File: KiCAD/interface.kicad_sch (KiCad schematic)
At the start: 3 parts, among them J4 8P8C_Shielded

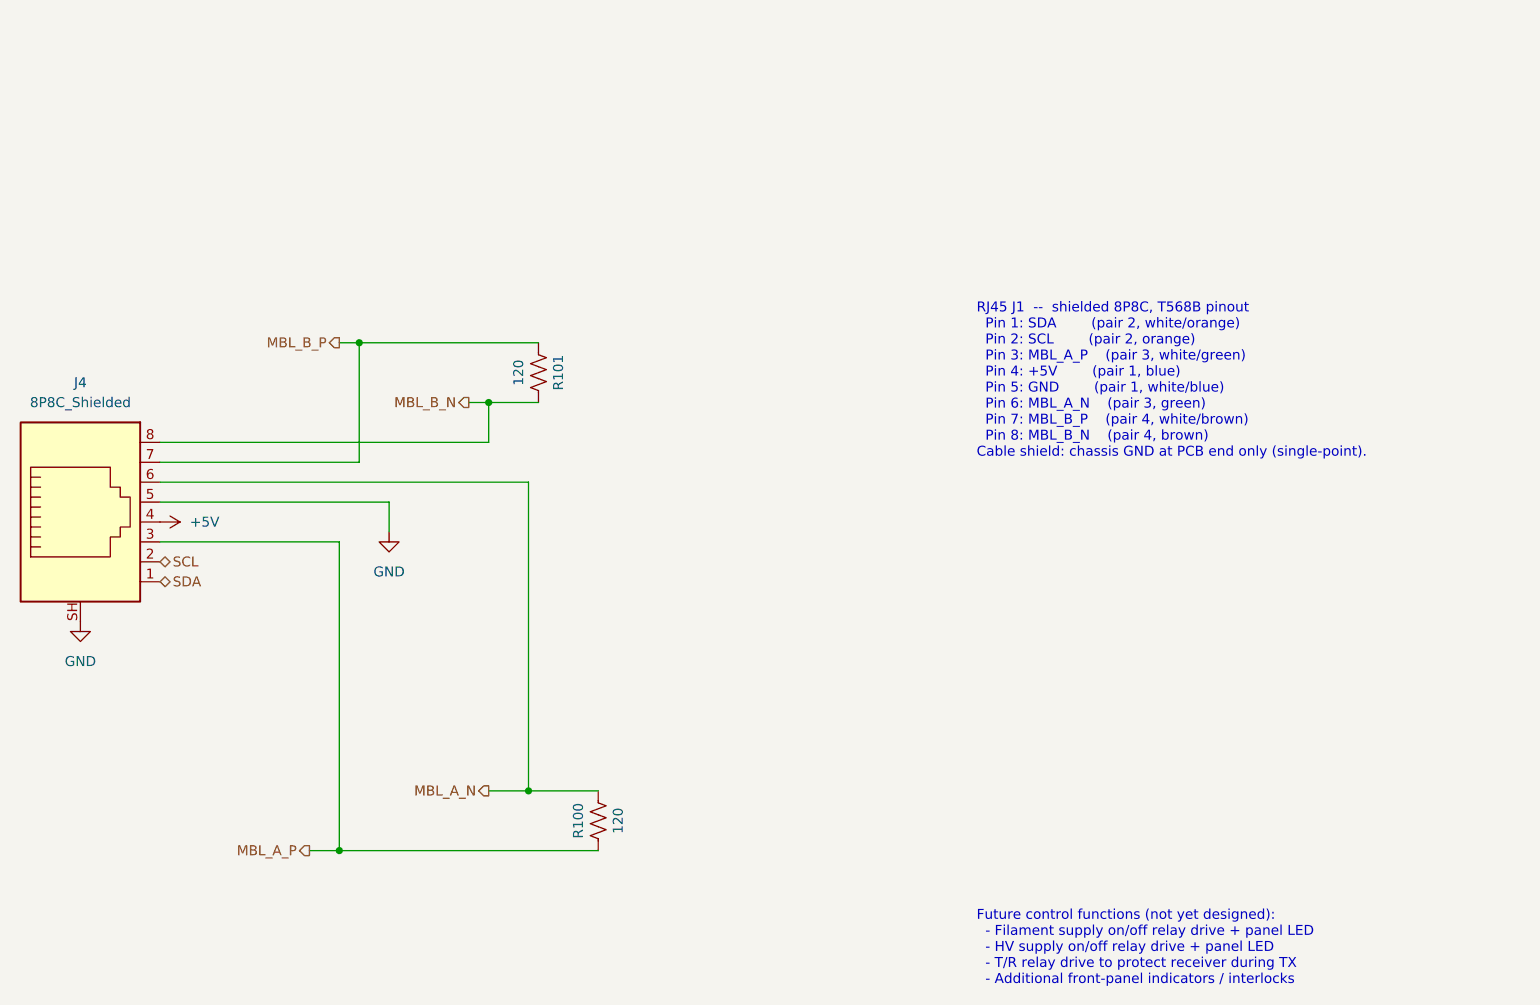
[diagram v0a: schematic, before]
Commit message: interface+arduino: wire the MBL-600 signal chain end-to-end
Interface sheet — receiver + termination + level-shift, all live:
  - RJ45 J1 (shielded 8P8C, Connector library symbol) instantiated with
    hierarchical labels on all eight positions per T568B; RJ45 pins
    3/6/7/8 land on MBL_A_P/N and MBL_B_P/N at the receiver-input side
  - R100 = R101 = 120 Ohm across the differential pairs (RS-422
    termination at the receiver end)
  - AM26LS32ACN (U15) at (119.38, 104.14); ch 1 handles MBL_A±, ch 2
    handles MBL_B±
  - Both enable pins tied to GND. ~G at pin 4 is the active-LOW
    enable, so GND puts it in its active state and turns on all four
    receivers per the datasheet's OR-logic gate (the other enable at
    pin 12 stays inactive at GND, but that is fine -- either one active
    is enough). GND was chosen over VCC purely for routing ease --
    GND fill will be closer than +5V traces at layout time
  - 2.2K + 10K voltage divider on each channel output (R26+R28 for A,
    R27+R29 for B). Ratio 10/12.2 = 0.82 drops the ~3.4 V TTL to
    ~2.79 V at the divider midpoint, comfortably below the ESP32
    absolute-max of 3.6 V and comfortably above V_IH_min (~2.475 V)
  - MBL600_A and MBL600_B hierarchical labels attached at the divider
    midpoints (not at the receiver 1Y/2Y pins) so the divided signal is
    what leaves the sheet
  - VCC (pin 16) wired to +5V, bypassed by 10 uF electrolytic + 100 nF
    ceramic (datasheet requires only 0.1 uF minimum; the 10 uF is
    just bonus bulk)
  - Unused channels 3&4 A/B inputs and 3Y/4Y outputs left unconnected
    per datasheet allowance

Arduino sheet:
  - MBL600_A hierarchical label at Metro D2, MBL600_B at Metro D3 --
    matches the FREQ_A / FREQ_B slots that the Metro symbol reserved
  - I_CATHODE_A moved from A0 (ADC2) to D8 (ADC1)
  - I_CATHODE_B moved from A1 (ADC2) to D9 (ADC1) -- both now on ADC1
    per the cathode-monitor design decision; the old A0/A1 assignment
    would have conflicted with WiFi/BL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
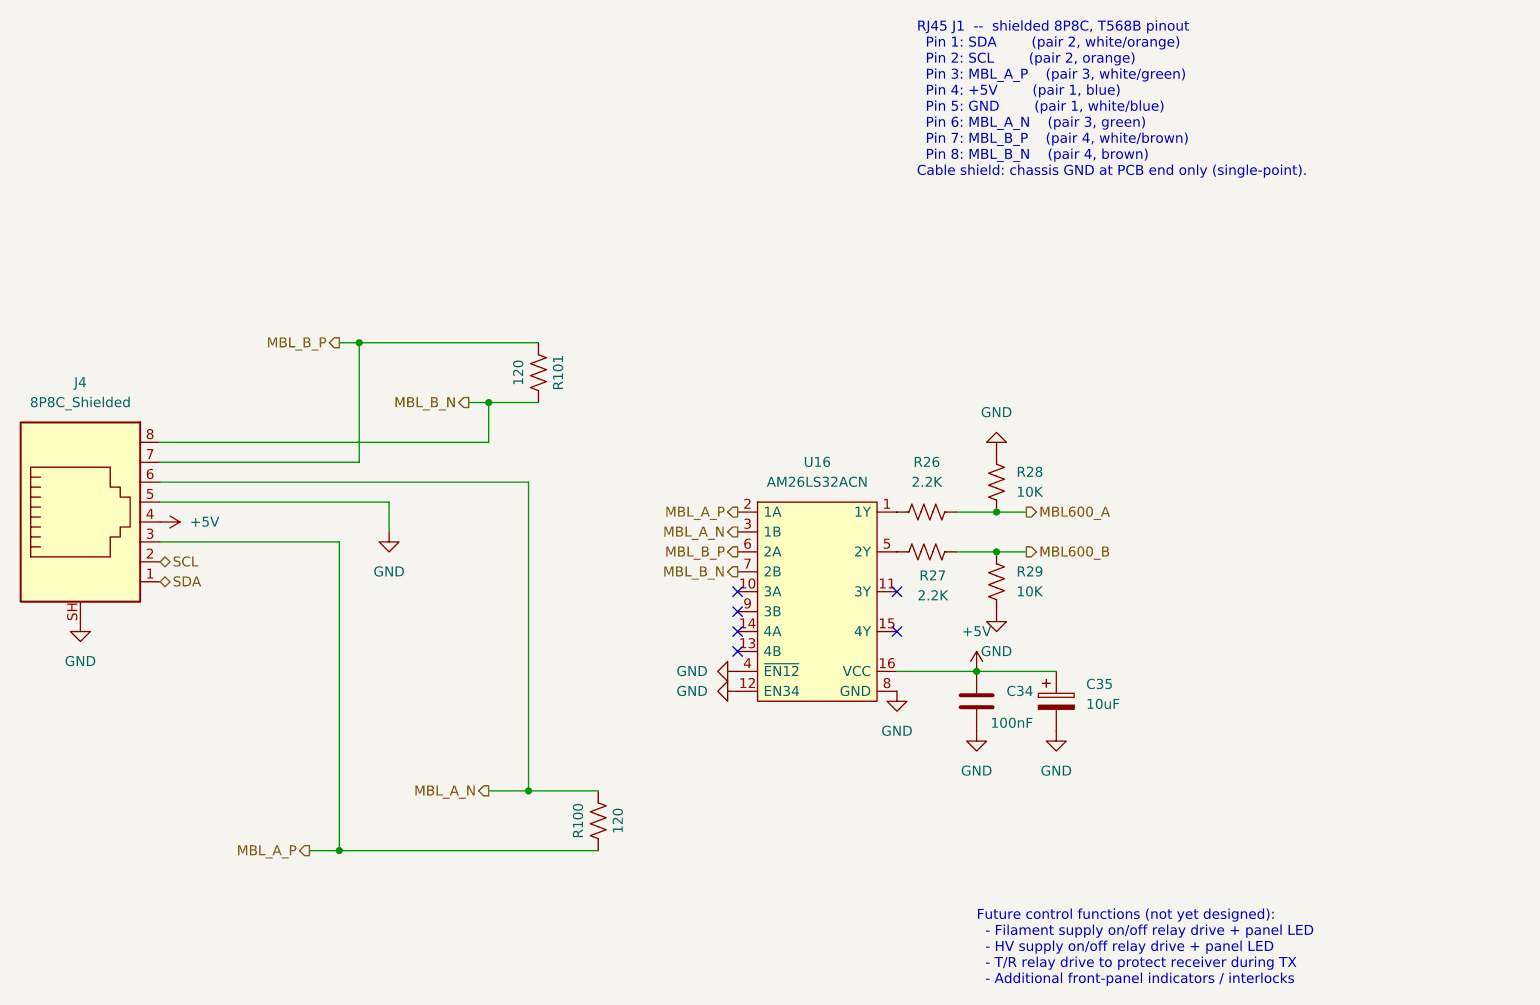
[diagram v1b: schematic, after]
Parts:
- added C34: 100nF, symbol Device:C
- added C35: 10uF, symbol Device:C_Polarized
- added R26, R27: 2.2K, symbol Device:R_US
- added R28, R29: 10K, symbol Device:R_US
- added U16: AM26LS32ACN, Package_DIP:DIP-16_W7.62mm, symbol xmitter:AM26LS32ACN
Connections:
- net +5V: now also C34.1, C35.1, U16.16 (VCC)
- net GND: now also C34.2, C35.2, R28.1, R29.2, U16.12 (EN34), U16.4 (~{EN12}), U16.8 (GND)
- net MBL_A_N: now also U16.3 (1B)
- net MBL_A_P: now also U16.2 (1A)
- net MBL_B_N: now also U16.7 (2B)
- net MBL_B_P: now also U16.6 (2A)
- new net: R26.1, U16.1 (1Y)
- new net: R27.1, U16.5 (2Y)
- new net MBL600_A: R26.2, R28.2
- new net MBL600_B: R27.2, R29.1
- no-connect marks 0 -> 6

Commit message: kicad: fill missing footprints across active sheets + MCP4728 breakout footprint
Footprint sweep across the analog control board sheets. All active sheets
now clean except U2 (Metro), which is intentionally off-PCB per the
Wingshield-plus-jumpers connection strategy.

Auto-assigned via tools/assign_cap_footprints.py:
  - buffer_keyer: C39, C40 (100 nF, THT disc D5.0mm P5.00mm) -- the null-
    trim bypass caps at R_INJ1 / R_INJ2 that ground the DAC output side
    of the 330K injection resistors going into T1 and T2
  - arduino: C36, C38 (100 nF THT disc), C37 (10 uF radial electrolytic)
  - interface: C34 (100 nF), C35 (10 uF)

Manual assignments:
  - interface: R26, R27, R28, R29 -> R_Axial_DIN0207_L6.3mm axial THT
    (matching the other 1/4W metal-film resistors used throughout)
  - interface: J4 (RJ45 socket) -> xmitter:Amphenol_RJE1D-188_Horizontal_Shielded
  - arduino: J6, J7, J8, J9, J10 -> PinHeader_1x02_P2.54mm_Vertical
  - buffer_keyer: U8 (MCP4728 breakout) -> new custom footprint

New custom footprint xmitter:Adafruit_MCP4728_Breakout:
  - Board 1.00 x 0.70 in (25.4 x 17.78 mm)
  - Four NPTH 2.5 mm mounting holes on 0.80 x 0.50 in spacing
  - 10 THT pads in two rows of 5, pad numbers match the xmitter:MCP4728
    symbol (1=VIN, 2=GND, 3=SCL, 4=SDA, 5=LDAC, 6=RDY, 7=VA, 8=VB, 9=VC,
    10=VD)
  - Pins 3 (SCL) and 4 (SDA) will be left unrouted on the parent PCB
    per the STEMMA QT daisy-chain topology decision -- I2C reaches the
    MCP4728 via a STEMMA cable from the Si5351 breakout, not via PCB
    traces
  - descr field flags "VERIFY silk-label to pad-number correspondence
    against the physical breakout before routing" -- Adafruit revisions
    vary and the specific row assignment was inferred from the
    datasheet fab print on page 20 plus the symbol pin numbering

Also committing Documentation/Components/MCP4728_datasheet.pdf and
Documentation/Components/cd4050b.pdf datasheets that were sitting
uncommitted.

Co-Authored-By: Claude Opus 4.7 <nor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
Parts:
- C34: footprint (none) -> Capacitor_THT:C_Disc_D5.0mm_W2.5mm_P5.00mm
- C35: footprint (none) -> Capacitor_THT:CP_Radial_D5.0mm_P2.00mm
- J4: footprint (none) -> xmitter:Amphenol_RJE1D-188_Horizontal_Shielded
- R26, R27, R28, R29: footprint (none) -> Resistor_THT:R_Axial_DIN0207_L6.3mm_D2.5mm_P10.16mm_Horizontal
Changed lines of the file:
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@@
 			)
 		)
-		(property "Footprint" ""
+		(property "Footprint" "Resistor_THT:R_Axial_DIN0207_L6.3mm_D2.5mm_P10.16mm_Horizontal"
 			(at 133.604 91.694 90)
 			(hide yes)
@@
 			)
 		)
-		(property "Footprint" ""
+		(property "Footprint" "Resistor_THT:R_Axial_DIN0207_L6.3mm_D2.5mm_P10.16mm_Horizontal"
 			(at 133.604 96.774 90)
 			(hide yes)
@@
 			)
 		)
-		(property "Footprint" ""
+		(property "Footprint" "Resistor_THT:R_Axial_DIN0207_L6.3mm_D2.5mm_P10.16mm_Horizontal"
 			(at 143.256 101.854 90)
 			(hide yes)
@@
 			)
 		)
-		(property "Footprint" ""
+		(property "Footprint" "Capacitor_THT:CP_Radial_D5.0mm_P2.00mm"
 			(at 150.8252 120.65 0)
 			(hide yes)
@@
 			)
 		)
-		(property "Footprint" ""
+		(property "Footprint" "Capacitor_THT:C_Disc_D5.0mm_W2.5mm_P5.00mm"
 			(at 140.6652 120.65 0)
 			(hide yes)
@@
 			)
 		)
-		(property "Footprint" ""
+		(property "Footprint" "Resistor_THT:R_Axial_DIN0207_L6.3mm_D2.5mm_P10.16mm_Horizontal"
 			(at 143.256 89.154 90)
 			(hide yes)
@@
 			)
 		)
-		(property "Footprint" ""
+		(property "Footprint" "xmitter:Amphenol_RJE1D-188_Horizontal_Shielded"
 			(at 25.4 93.345 90)
 			(hide yes)

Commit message: schematic: I2C topology flip + CD14538B heartbeat + pre-layout audit
- Documentation updates for the STEMMA-QT topology flip (MCP4728 upstream
  of Si5351): design_review_7-5-26 C1 marked resolved, build_checklist
  Phase 1 gets the 6-step first-boot procedure, cw_envelope_keyer I2C
  address section rewritten, front_panel_interface signal-chain diagram
  refreshed.
- CD14538B dual retriggerable monostable added to xmitter.kicad_sym
  (PDIP-16, pinout verified against datasheet fig. 1), plus datasheet
  file.
- Arduino sheet: CD14538B heartbeat topology on Q5 HV contactor -- U18
  + R30 470K + C41 1uF timing (t_w ~470 ms), Q7 series FET stack,
  C42/C43 VDD bypass and bulk.
- Pre-layout audit output as Documentation/punch_list_7-6-26.txt (list
  of blockers before PCB layout, ordered by severity).

Co-Authored-By: Claude Opus 4.7 (1M context) <noreply@anthropic.com>
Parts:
- added J15: Conn_01x03_Pin, symbol Connector:Conn_01x03_Pin
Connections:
- net GND: now also J15.1 (Pin_1)
- net MBL600_A: now also J15.3 (Pin_3)
- net MBL600_B: now also J15.2 (Pin_2)
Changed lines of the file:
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@@
+	)
+	(junction
+		(at 151.13 97.79)
+		(diameter 0)
+		(color 0 0 0 0)
+	)
+	(junction
+		(at 170.18 92.71)
+		(diameter 0)
+		(color 0 0 0 0)
 	)
 	(junction
@@
 	)
 	(junction
-		(at 142.24 97.79)
+		(at 142.24 92.71)
 		(diameter 0)
 		(color 0 0 0 0)
@@
 	)
 	(junction
-		(at 142.24 92.71)
+		(at 142.24 97.79)
 		(diameter 0)
 		(color 0 0 0 0)
@@
 	(wire
 		(pts
-			(xy 146.05 92.71) (xy 142.24 92.71)
+			(xy 173.99 92.71) (xy 170.18 92.71)
+		)
+		(stroke
+			(width 0)
+			(type default)
+		)
+	)
+	(wire
+		(pts
+			(xy 170.18 92.71) (xy 170.18 102.87)
 		)
 		(stroke
@@
 	(wire
 		(pts
+			(xy 151.13 97.79) (xy 142.24 97.79)
+		)
+		(stroke
+			(width 0)
+			(type default)
+		)
+	)
+	(wire
+		(pts
 			(xy 64.77 91.44) (xy 64.77 95.25)
 		)
@@
 	(wire
 		(pts
+			(xy 170.18 92.71) (xy 142.24 92.71)
+		)
+		(stroke
+			(width 0)
+			(type default)
+		)
+	)
+	(wire
+		(pts
 			(xy 35.56 96.52) (xy 58.42 96.52)
 		)
@@
 	(wire
 		(pts
-			(xy 146.05 97.79) (xy 142.24 97.79)
+			(xy 153.67 97.79) (xy 151.13 97.79)
+		)
+		(stroke
+			(width 0)
+			(type default)
+		)
+	)
+	(wire
+		(pts
+			(xy 151.13 105.41) (xy 151.13 97.79)
 		)
 		(stroke
@@
 		(pts
 			(xy 58.42 96.52) (xy 58.42 135.89)
+		)
+		(stroke
+			(width 0)
+			(type default)
+		)
+	)
+	(wire
+		(pts
+			(xy 170.18 105.41) (xy 151.13 105.41)
 		)
 		(stroke
@@
 	(hierarchical_label "MBL600_B"
 		(shape output)
-		(at 146.05 97.79 0)
+		(at 153.67 97.79 0)
 		(effects
 			(font
@@
 	(hierarchical_label "MBL600_A"
 		(shape output)
-		(at 146.05 92.71 0)
+		(at 173.99 92.71 0)
 		(effects
 			(font
@@
 					(unit 1)
 				)
+			)
+		)
+	)
+	(symbol
+		(lib_id "Connector:Conn_01x03_Pin")
+		(at 175.26 105.41 180)
+		(unit 1)
+		(body_style 1)
+		(exclude_from_sim no)
+		(in_bom yes)
+		(on_board yes)
+		(in_pos_files yes)
+		(dnp no)
+		(fields_autoplaced yes)
+		(property "Reference" "J15"
+			(at 176.53 104.1399 0)
+			(show_name no)
+			(do_not_autoplace no)
+			(effects
+				(font
+					(size 1.27 1.27)
+				)
+				(justify right)
+			)
+		)
+		(property "Value" "Conn_01x03_Pin"
+			(at 176.53 106.6799 0)
+			(show_name no)
+			(do_not_autoplace no)
+			(effects
+				(font
+					(size 1.27 1.27)
+				)
+				(justify right)
+			)
+		)
+		(property "Footprint" ""
+			(at 175.26 105.41 0)
+			(hide yes)
+			(show_name no)
+			(do_not_autoplace no)
+			(effects
+				(font
+					(size 1.27 1.27)
+				)
+			)
+		)
+		(property "Datasheet" ""
+			(at 175.26 105.41 0)
+			(hide yes)
+			(show_name no)
+			(do_not_autoplace no)
+			(effects
+				(font
+					(size 1.27 1.27)
+				)
+			)
+		)
+		(property "Description" "Generic connector, single row, 01x03, script generated"
+			(at 175.26 105.41 0)
+			(hide yes)
+			(show_name no)
+			(do_not_autoplace no)
+			(effects
+				(font
+					(size 1.27 1.27)
+				)
+			)
+		)
+		(pin "2"
+		)
+		(pin "1"
+		)
+		(pin "3"
+		)
+		(instances
+			(project "KiCAD"
+				(path "/d3de40b8-856b-4fbd-829c-f45ffcd55742/5c3f4a2b-7d1e-4f8b-9c6d-0e8a1b2c3d4e"
+					(reference "J15")
+					(unit 1)
+				)
+			)
+		)
+	)
+	(symbol
+		(lib_id "power:GND")
+		(at 170.18 107.95 0)
+		(unit 1)
+		(body_style 1)
+		(exclude_from_sim no)
+		(in_bom yes)
+		(on_board yes)
+		(in_pos_files yes)
+		(dnp no)
+		(fields_autoplaced yes)
+		(property "Reference" "#PWR0119"
+			(at 170.18 114.3 0)
+			(hide yes)
+			(show_name no)
+			(do_not_autoplace no)
+			(effects
+				(font
+					(size 1.27 1.27)
+				)
+			)
+		)
+		(property "Value" "GND"
+			(at 170.18 113.03 0)
+			(show_name no)
+			(do_not_autoplace no)
+			(effects
+				(font
+					(size 1.27 1.27)
+				)
+			)
+		)
+		(property "Footprint" ""
+			(at 170.18 107.95 0)
+			(hide yes)
+			(show_name no)
+			(do_not_autoplace no)
+			(effects
+				(font
+					(size 1.27 1.27)
+				)
+			)
+		)
+		(property "Datasheet" ""
+			(at 170.18 107.95 0)
+			(hide yes)
+			(show_name no)
+			(do_not_autoplace no)
+			(effects
+				(font
+					(size 1.27 1.27)
+				)
+			)
+		)
+		(property "Description" "Power symbol creates a global label with name \"GND\" , ground"
+			(at 170.18 107.95 0)
+			(hide yes)
+			(show_name no)
+			(do_not_autoplace no)
+			(effects
+				(font
+					(size 1.27 1.27)
+				)
+			)
+		)
+		(pin "1"
+		)
+		(instances
+			(project "KiCAD"
+				(path "/d3de40b8-856b-4fbd-829c-f45ffcd55742/5c3f4a2b-7d1e-4f8b-9c6d-0e8a1b2c3d4e"
+					(reference "#PWR0119")
+					(unit 1)
+				)
